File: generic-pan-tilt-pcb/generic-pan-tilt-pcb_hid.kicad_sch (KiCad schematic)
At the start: 10 parts, among them SW3 SW_DIP_x12, U5 MCP23017_SO

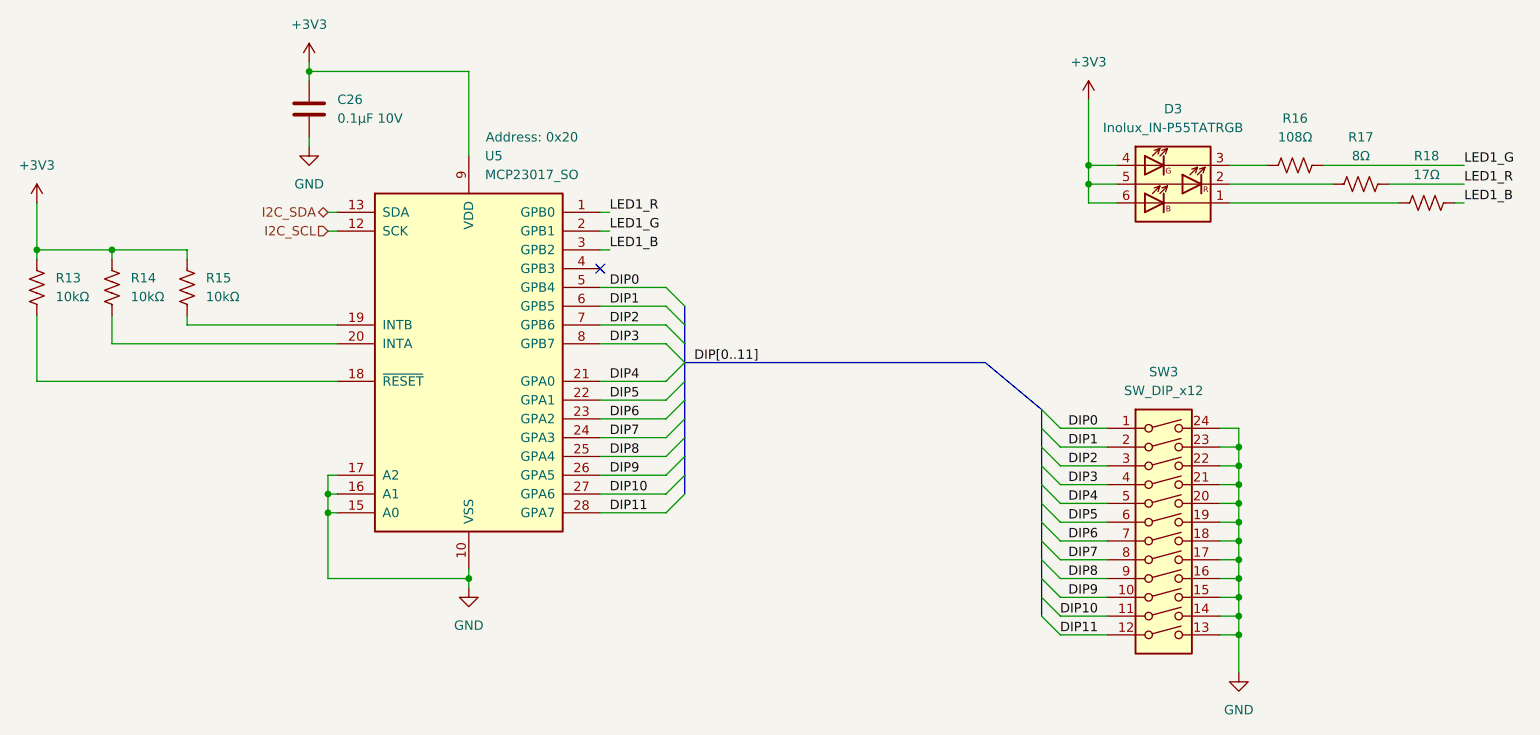
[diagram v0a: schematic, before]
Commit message: pick all footprints, begin layout
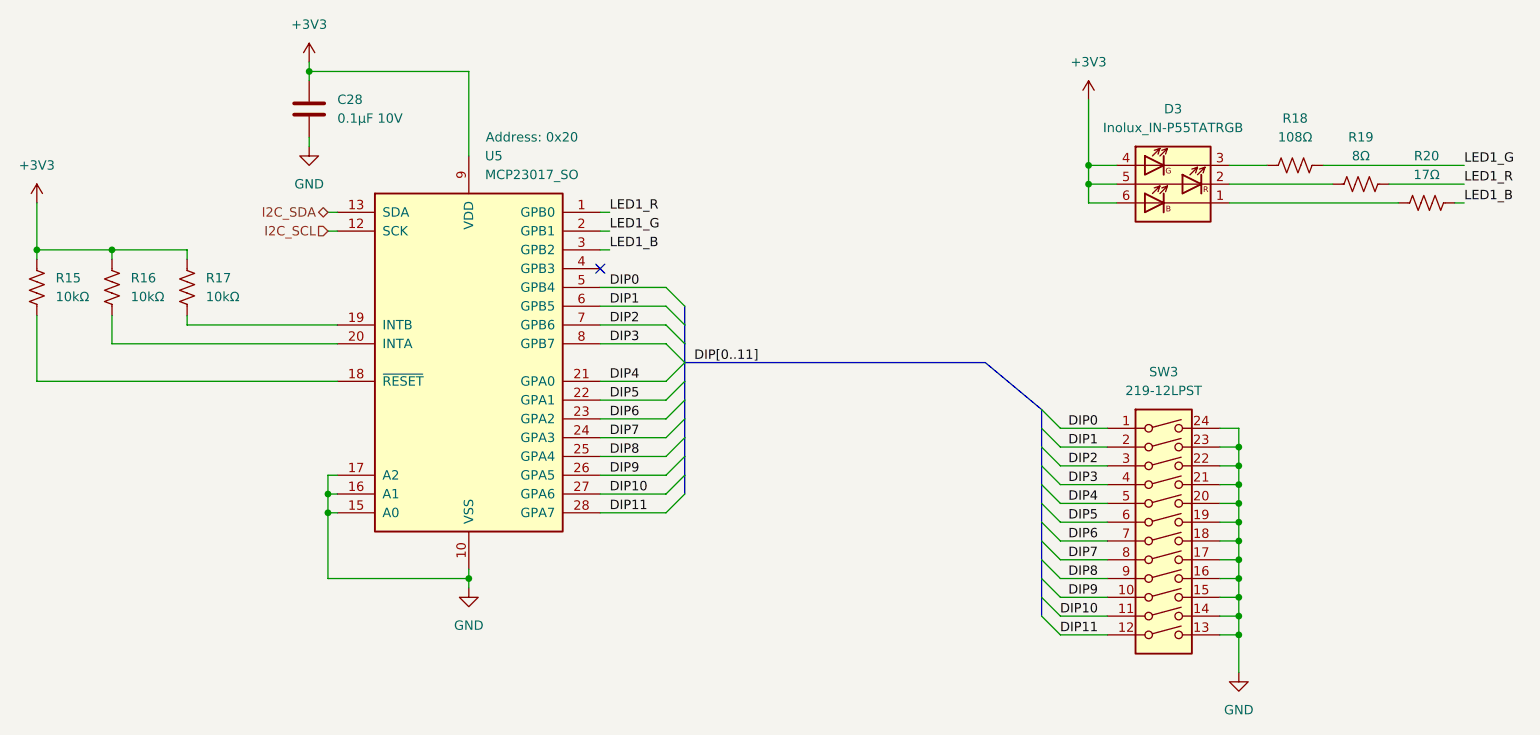
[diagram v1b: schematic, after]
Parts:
- C28: renamed from C26; footprint (none) -> Capacitor_SMD:C_0603_1608Metric
- R15: renamed from R13; footprint (none) -> Resistor_SMD:R_0603_1608Metric
- R16: renamed from R14; footprint (none) -> Resistor_SMD:R_0603_1608Metric
- R17: renamed from R15; footprint (none) -> Resistor_SMD:R_0603_1608Metric
- R18: renamed from R16; footprint (none) -> Resistor_SMD:R_0603_1608Metric
- R19: renamed from R17; footprint (none) -> Resistor_SMD:R_0603_1608Metric
- R20: renamed from R18; footprint (none) -> Resistor_SMD:R_0603_1608Metric
- SW3: value SW_DIP_x12 -> 219-12LPST; footprint (none) -> Button_Switch_SMD:SW_DIP_SPSTx12_Slide_6.7x32.04mm_W8.61mm_P2.54mm_LowProfile
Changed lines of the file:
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@@
 		(dnp no)
 		(fields_autoplaced yes)
-		(property "Reference" "R17"
+		(property "Reference" "R19"
 			(at 231.14 50.8 90)
 			(effects
@@
 			)
 		)
-		(property "Footprint" ""
+		(property "Footprint" "Resistor_SMD:R_0603_1608Metric"
 			(at 231.394 56.134 90)
 			(effects
@@
 			(project "generic-pan-tilt-pcb"
 				(path "/e3bbbe58-bf8f-42a8-8505-028de8235dc1/58e8aa21-838b-4e25-b5a5-dc2029ad2cce"
-					(reference "R17")
+					(reference "R19")
 					(unit 1)
 				)
@@
 		(dnp no)
 		(fields_autoplaced yes)
-		(property "Reference" "R15"
+		(property "Reference" "R17"
 			(at 74.93 69.8499 0)
 			(effects
@@
 			)
 		)
-		(property "Footprint" ""
+		(property "Footprint" "Resistor_SMD:R_0603_1608Metric"
 			(at 73.406 71.374 90)
 			(effects
@@
 			(project "generic-pan-tilt-pcb"
 				(path "/e3bbbe58-bf8f-42a8-8505-028de8235dc1/58e8aa21-838b-4e25-b5a5-dc2029ad2cce"
-					(reference "R15")
+					(reference "R17")
 					(unit 1)
 				)
@@
 		(dnp no)
 		(fields_autoplaced yes)
-		(property "Reference" "#PWR069"
+		(property "Reference" "#PWR068"
 			(at 214.63 129.54 0)
 			(effects
@@
 			(project "generic-pan-tilt-pcb"
 				(path "/e3bbbe58-bf8f-42a8-8505-028de8235dc1/58e8aa21-838b-4e25-b5a5-dc2029ad2cce"
-					(reference "#PWR069")
+					(reference "#PWR068")
 					(unit 1)
 				)
@@
 		(dnp no)
 		(fields_autoplaced yes)
-		(property "Reference" "#PWR067"
+		(property "Reference" "#PWR066"
 			(at 110.49 118.11 0)
 			(effects
@@
 			(project "generic-pan-tilt-pcb"
 				(path "/e3bbbe58-bf8f-42a8-8505-028de8235dc1/58e8aa21-838b-4e25-b5a5-dc2029ad2cce"
-					(reference "#PWR067")
+					(reference "#PWR066")
 					(unit 1)
 				)
@@
 			)
 		)
-		(property "Value" "SW_DIP_x12"
+		(property "Value" "219-12LPST"
 			(at 204.47 85.09 0)
 			(effects
@@
 			)
 		)
-		(property "Footprint" ""
+		(property "Footprint" "Button_Switch_SMD:SW_DIP_SPSTx12_Slide_6.7x32.04mm_W8.61mm_P2.54mm_LowProfile"
 			(at 204.47 105.41 0)
 			(effects
@@
 		(dnp no)
 		(fields_autoplaced yes)
-		(property "Reference" "#PWR065"
+		(property "Reference" "#PWR064"
 			(at 88.9 44.45 0)
 			(effects
@@
 			(project "generic-pan-tilt-pcb"
 				(path "/e3bbbe58-bf8f-42a8-8505-028de8235dc1/58e8aa21-838b-4e25-b5a5-dc2029ad2cce"
-					(reference "#PWR065")
+					(reference "#PWR064")
 					(unit 1)
 				)
@@
 		(dnp no)
 		(fields_autoplaced yes)
-		(property "Reference" "R13"
+		(property "Reference" "R15"
 			(at 54.61 69.8499 0)
 			(effects
@@
 			)
 		)
-		(property "Footprint" ""
+		(property "Footprint" "Resistor_SMD:R_0603_1608Metric"
 			(at 53.086 71.374 90)
 			(effects
@@
 			(project "generic-pan-tilt-pcb"
 				(path "/e3bbbe58-bf8f-42a8-8505-028de8235dc1/58e8aa21-838b-4e25-b5a5-dc2029ad2cce"
-					(reference "R13")
+					(reference "R15")
 					(unit 1)
 				)
@@
 		(dnp no)
 		(fields_autoplaced yes)
-		(property "Reference" "R16"
+		(property "Reference" "R18"
 			(at 222.25 48.26 90)
 			(effects
@@
 			)
 		)
-		(property "Footprint" ""
+		(property "Footprint" "Resistor_SMD:R_0603_1608Metric"
 			(at 221.996 55.626 90)
 			(effects
@@
 			(project "generic-pan-tilt-pcb"
 				(path "/e3bbbe58-bf8f-42a8-8505-028de8235dc1/58e8aa21-838b-4e25-b5a5-dc2029ad2cce"
-					(reference "R16")
+					(reference "R18")
 					(unit 1)
 				)
@@
 		(dnp no)
 		(fields_autoplaced yes)
-		(property "Reference" "#PWR068"
+		(property "Reference" "#PWR067"
 			(at 194.31 49.53 0)
 			(effects
@@
 			(project "generic-pan-tilt-pcb"
 				(path "/e3bbbe58-bf8f-42a8-8505-028de8235dc1/58e8aa21-838b-4e25-b5a5-dc2029ad2cce"
-					(reference "#PWR068")
+					(reference "#PWR067")
 					(unit 1)
 				)
@@
 		(dnp no)
 		(fields_autoplaced yes)
-		(property "Reference" "#PWR064"
+		(property "Reference" "#PWR063"
 			(at 52.07 63.5 0)
 			(effects
@@
 			(project "generic-pan-tilt-pcb"
 				(path "/e3bbbe58-bf8f-42a8-8505-028de8235dc1/58e8aa21-838b-4e25-b5a5-dc2029ad2cce"
-					(reference "#PWR064")
+					(reference "#PWR063")
 					(unit 1)
 				)
@@
 		(dnp no)
 		(fields_autoplaced yes)
-		(property "Reference" "C26"
+		(property "Reference" "C28"
 			(at 92.71 45.7199 0)
 			(effects
@@
 			)
 		)
-		(property "Footprint" ""
+		(property "Footprint" "Capacitor_SMD:C_0603_1608Metric"
 			(at 89.8652 50.8 0)
 			(effects
@@
 			(project "generic-pan-tilt-pcb"
 				(path "/e3bbbe58-bf8f-42a8-8505-028de8235dc1/58e8aa21-838b-4e25-b5a5-dc2029ad2cce"
-					(reference "C26")
+					(reference "C28")
 					(unit 1)
 				)
@@
 		(dnp no)
 		(fields_autoplaced yes)
-		(property "Reference" "R14"
+		(property "Reference" "R16"
 			(at 64.77 69.8499 0)
 			(effects
@@
 			)
 		)
-		(property "Footprint" ""
+		(property "Footprint" "Resistor_SMD:R_0603_1608Metric"
 			(at 63.246 71.374 90)
 			(effects
@@
 			(project "generic-pan-tilt-pcb"
 				(path "/e3bbbe58-bf8f-42a8-8505-028de8235dc1/58e8aa21-838b-4e25-b5a5-dc2029ad2cce"
-					(reference "R14")
+					(reference "R16")
 					(unit 1)
 				)
@@
 		(dnp no)
 		(fields_autoplaced yes)
-		(property "Reference" "#PWR066"
+		(property "Reference" "#PWR065"
 			(at 88.9 58.42 0)
 			(effects
@@
 			(project "generic-pan-tilt-pcb"
 				(path "/e3bbbe58-bf8f-42a8-8505-028de8235dc1/58e8aa21-838b-4e25-b5a5-dc2029ad2cce"
-					(reference "#PWR066")
+					(reference "#PWR065")
 					(unit 1)
 				)
@@
 		(dnp no)
 		(fields_autoplaced yes)
-		(property "Reference" "R18"
+		(property "Reference" "R20"
 			(at 240.03 53.34 90)
 			(effects
@@
 			)
 		)
-		(property "Footprint" ""
+		(property "Footprint" "Resistor_SMD:R_0603_1608Metric"
 			(at 240.284 58.674 90)
 			(effects
@@
 			(project "generic-pan-tilt-pcb"
 				(path "/e3bbbe58-bf8f-42a8-8505-028de8235dc1/58e8aa21-838b-4e25-b5a5-dc2029ad2cce"
-					(reference "R18")
-					(unit 1)
-				)
+					(reference "R20")
+					(unit 1)
+				)

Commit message: more progress
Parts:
- removed D3: Inolux_IN-P55TATRGB, LED_SMD:LED_Inolux_IN-P55TATRGB_PLCC6_5.0x5.5mm_P1.8mm, symbol LED:Inolux_IN-P55TATRGB
- removed R19: 8Ω, Resistor_SMD:R_0603_1608Metric, symbol Device:R_US
- added D3: LTST-C235KGKRKT, LED_SMD:LED_LiteOn_LTST-C235KGKRKT, symbol LED:LTST-C235KGKRKT
- renumbered R20 to R19
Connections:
- net +3V3: now also D3.2 (A2), D3.3 (A1)
- net LED1_G: now also R19.2; no longer R18.1
- net LED1_R: now also R18.1
- net at R18.2: now also D3.4 (K1)
- net at R19.1: now also D3.1 (K2)
- net LED1_B: no longer names the net of U5.3 (GPB2)
- net LED1_B: no longer R19.2
- no-connect marks 1 -> 2
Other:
- moved on the sheet: R19
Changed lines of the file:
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@@
-	)
-	(junction
-		(at 194.31 57.15)
-		(diameter 0)
-		(color 0 0 0 0)
 	)
 	(junction
@@
 		(at 128.27 68.58)
 	)
+	(no_connect
+		(at 128.27 66.04)
+	)
 	(bus_entry
 		(at 187.96 97.79)
@@
 	(wire
 		(pts
-			(xy 213.36 57.15) (xy 227.33 57.15)
-		)
-		(stroke
-			(width 0)
-			(type default)
-		)
-	)
-	(wire
-		(pts
 			(xy 88.9 40.64) (xy 88.9 41.91)
 		)
@@
 	(wire
 		(pts
-			(xy 226.06 54.61) (xy 245.11 54.61)
-		)
-		(stroke
-			(width 0)
-			(type default)
-		)
-	)
-	(wire
-		(pts
 			(xy 214.63 107.95) (xy 214.63 110.49)
 		)
@@
 	(wire
 		(pts
-			(xy 243.84 59.69) (xy 245.11 59.69)
+			(xy 232.41 59.69) (xy 233.68 59.69)
 		)
 		(stroke
@@
 	(wire
 		(pts
-			(xy 213.36 59.69) (xy 236.22 59.69)
+			(xy 213.36 59.69) (xy 224.79 59.69)
 		)
 		(stroke
@@
 	(wire
 		(pts
+			(xy 226.06 54.61) (xy 233.68 54.61)
+		)
+		(stroke
+			(width 0)
+			(type default)
+		)
+	)
+	(wire
+		(pts
 			(xy 128.27 91.44) (xy 137.16 91.44)
 		)
@@
 	(wire
 		(pts
-			(xy 234.95 57.15) (xy 245.11 57.15)
-		)
-		(stroke
-			(width 0)
-			(type default)
-		)
-	)
-	(wire
-		(pts
 			(xy 212.09 107.95) (xy 214.63 107.95)
 		)
@@
 	(wire
 		(pts
-			(xy 194.31 57.15) (xy 194.31 59.69)
+			(xy 194.31 54.61) (xy 194.31 59.69)
 		)
 		(stroke
@@
 		)
 	)
-	(wire
-		(pts
-			(xy 194.31 57.15) (xy 198.12 57.15)
-		)
-		(stroke
-			(width 0)
-			(type default)
-		)
-	)
 	(bus
 		(pts
@@
 	(wire
 		(pts
-			(xy 128.27 66.04) (xy 129.54 66.04)
-		)
-		(stroke
-			(width 0)
-			(type default)
-		)
-	)
-	(wire
-		(pts
 			(xy 128.27 83.82) (xy 137.16 83.82)
 		)
@@
 		(pts
 			(xy 212.09 92.71) (xy 214.63 92.71)
-		)
-		(stroke
-			(width 0)
-			(type default)
-		)
-	)
-	(wire
-		(pts
-			(xy 194.31 54.61) (xy 194.31 57.15)
 		)
 		(stroke
@@
 		)
 	)
-	(label "LED1_B"
-		(at 245.11 59.69 0)
-		(fields_autoplaced yes)
-		(effects
-			(font
-				(size 1.27 1.27)
-			)
-			(justify left bottom)
-		)
-	)
 	(label "DIP9"
 		(at 129.54 96.52 0)
@@
 		)
 	)
-	(label "LED1_B"
-		(at 129.54 66.04 0)
-		(fields_autoplaced yes)
-		(effects
-			(font
-				(size 1.27 1.27)
-			)
-			(justify left bottom)
-		)
-	)
 	(label "DIP8"
 		(at 129.54 93.98 0)
@@
 	)
 	(label "LED1_G"
-		(at 245.11 54.61 0)
+		(at 233.68 59.69 0)
 		(fields_autoplaced yes)
 		(effects
@@
 	)
 	(label "LED1_R"
-		(at 245.11 57.15 0)
+		(at 233.68 54.61 0)
 		(fields_autoplaced yes)
 		(effects
@@
 			)
 			(justify right)
-		)
-	)
-	(symbol
-		(lib_id "Device:R_US")
-		(at 231.14 57.15 90)
-		(unit 1)
-		(exclude_from_sim no)
-		(in_bom yes)
-		(on_board yes)
-		(dnp no)
-		(fields_autoplaced yes)
-		(property "Reference" "R19"
-			(at 231.14 50.8 90)
-			(effects
-				(font
-					(size 1.27 1.27)
-				)
-			)
-		)
-		(property "Value" "8Ω"
-			(at 231.14 53.34 90)
-			(effects
-				(font
-					(size 1.27 1.27)
-				)
-			)
-		)
-		(property "Footprint" "Resistor_SMD:R_0603_1608Metric"
-			(at 231.394 56.134 90)
-			(effects
-				(font
-					(size 1.27 1.27)
-				)
-				(hide yes)
-			)
-		)
-		(property "Datasheet" "~"
-			(at 231.14 57.15 0)
-			(effects
-				(font
-					(size 1.27 1.27)
-				)
-				(hide yes)
-			)
-		)
-		(property "Description" "Resistor, US symbol"
-			(at 231.14 57.15 0)
-			(effects
-				(font
-					(size 1.27 1.27)
-				)
-				(hide yes)
-			)
-		)
-		(pin "1"
-		)
-		(pin "2"
-		)
-		(instances
-			(project "generic-pan-tilt-pcb"
-				(path "/e3bbbe58-bf8f-42a8-8505-028de8235dc1/58e8aa21-838b-4e25-b5a5-dc2029ad2cce"
-					(reference "R19")
-					(unit 1)
-				)
-			)
 		)
 	)
@@
 				(path "/e3bbbe58-bf8f-42a8-8505-028de8235dc1/58e8aa21-838b-4e25-b5a5-dc2029ad2cce"
 					(reference "R17")
+					(unit 1)
+				)
+			)
+		)
+	)
+	(symbol
+		(lib_id "LED:LTST-C235KGKRKT")
+		(at 205.74 57.15 0)
+		(unit 1)
+		(exclude_from_sim no)
+		(in_bom yes)
+		(on_board yes)
+		(dnp no)
+		(fields_autoplaced yes)
+		(property "Reference" "D3"
+			(at 205.74 45.72 0)
+			(effects
+				(font
+					(size 1.27 1.27)
+				)
+			)
+		)
+		(property "Value" "LTST-C235KGKRKT"
+			(at 205.74 48.26 0)
+			(effects
+				(font
+					(size 1.27 1.27)
+				)
+			)
+		)
+		(property "Footprint" "LED_SMD:LED_LiteOn_LTST-C235KGKRKT"
+			(at 206.502 57.15 0)
+			(effects
+				(font
+					(size 1.27 1.27)
+				)
+				(hide yes)
+			)
+		)
+		(property "Datasheet" "https://optoelectronics.liteon.com/upload/download/DS22-2009-0219/LTST-C235KGKRKT.pdf"
+			(at 206.502 57.15 0)
+			(effects
+				(font
+					(size 1.27 1.27)
+				)
+				(hide yes)
+			)
+		)
+		(property "Description" "LED dual red/green, 4-pin, down-facing"
+			(at 205.74 57.15 0)
+			(effects
+				(font
+					(size 1.27 1.27)
+				)
+				(hide yes)
+			)
+		)
+		(pin "2"
+		)
+		(pin "1"
+		)
+		(pin "4"
+		)
+		(pin "3"
+		)
+		(instances
+			(project ""
+				(path "/e3bbbe58-bf8f-42a8-8505-028de8235dc1/58e8aa21-838b-4e25-b5a5-dc2029ad2cce"
+					(reference "D3")
 					(unit 1)
 				)
@@
 	)
 	(symbol
-		(lib_id "LED:Inolux_IN-P55TATRGB")
-		(at 205.74 57.15 0)
-		(unit 1)
-		(exclude_from_sim no)
-		(in_bom yes)
-		(on_board yes)
-		(dnp no)
-		(fields_autoplaced yes)
-		(property "Reference" "D3"
-			(at 205.74 46.99 0)
-			(effects
-				(font
-					(size 1.27 1.27)
-				)
-			)
-		)
-		(property "Value" "Inolux_IN-P55TATRGB"
-			(at 205.74 49.53 0)
-			(effects
-				(font
-					(size 1.27 1.27)
-				)
-			)
-		)
-		(property "Footprint" "LED_SMD:LED_Inolux_IN-P55TATRGB_PLCC6_5.0x5.5mm_P1.8mm"
-			(at 200.66 65.278 0)
-			(effects
-				(font
-					(size 1.27 1.27)
-				)
-				(justify left)
-				(hide yes)
-			)
-		)
-		(property "Datasheet" "https://www.inolux-corp.com/datasheet/SMDLED/RGB%20Top%20View/IN-P55TATRGB.pdf"
-			(at 200.66 67.31 0)
-			(effects
-				(font
-					(size 1.27 1.27)
-				)
-				(justify left)
-				(hide yes)
-			)
-		)
-		(property "Description" "Inolux RGB LED, PLCC-6"
-			(at 205.74 57.15 0)
-			(effects
-				(font
-					(size 1.27 1.27)
-				)
-				(hide yes)
-			)
-		)
-		(pin "1"
-		)
-		(pin "4"
-		)
-		(pin "5"
-		)
-		(pin "3"
-		)
-		(pin "2"
-		)
-		(pin "6"
-		)
-		(instances
-			(project "generic-pan-tilt-pcb"
-				(path "/e3bbbe58-bf8f-42a8-8505-028de8235dc1/58e8aa21-838b-4e25-b5a5-dc2029ad2cce"
-					(reference "D3")
-					(unit 1)
-				)
-			)
-		)
-	)
-	(symbol
 		(lib_id "Device:C")
 		(at 88.9 46.99 0)
@@
 	(symbol
 		(lib_id "Device:R_US")
-		(at 240.03 59.69 90)
+		(at 228.6 59.69 90)
 		(unit 1)
 		(exclude_from_sim no)
@@
 		(dnp no)
 		(fields_autoplaced yes)
-		(property "Reference" "R20"
-			(at 240.03 53.34 90)
+		(property "Reference" "R19"
+			(at 228.6 53.34 90)
 			(effects
 				(font
@@
 		)
 		(property "Value" "17Ω"
-			(at 240.03 55.88 90)
+			(at 228.6 55.88 90)
 			(effects
 				(font
@@
 		)
 		(property "Footprint" "Resistor_SMD:R_0603_1608Metric"
-			(at 240.284 58.674 90)
+			(at 228.854 58.674 90)
 			(effects
 				(font
@@
 		)
 		(property "Datasheet" "~"
-			(at 240.03 59.69 0)
+			(at 228.6 59.69 0)
 			(effects
 				(font
@@
 		)
 		(property "Description" "Resistor, US symbol"
-			(at 240.03 59.69 0)
+			(at 228.6 59.69 0)
 			(effects
 				(font
@@
 			(project "generic-pan-tilt-pcb"
 				(path "/e3bbbe58-bf8f-42a8-8505-028de8235dc1/58e8aa21-838b-4e25-b5a5-dc2029ad2cce"
-					(reference "R20")
+					(reference "R19")
 					(unit 1)
 				)

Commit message: begin new routing
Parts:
- C28: footprint Capacitor_SMD:C_0603_1608Metric -> Capacitor_SMD:C_0402_1005Metric
- R15, R16, R17, R18, R19: footprint Resistor_SMD:R_0603_1608Metric -> Capacitor_SMD:C_0402_1005Metric
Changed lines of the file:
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@@
 			)
 		)
-		(property "Footprint" "Resistor_SMD:R_0603_1608Metric"
+		(property "Footprint" "Capacitor_SMD:C_0402_1005Metric"
 			(at 73.406 71.374 90)
 			(effects
@@
 			)
 		)
-		(property "Footprint" "Resistor_SMD:R_0603_1608Metric"
+		(property "Footprint" "Capacitor_SMD:C_0402_1005Metric"
 			(at 53.086 71.374 90)
 			(effects
@@
 			)
 		)
-		(property "Footprint" "Resistor_SMD:R_0603_1608Metric"
+		(property "Footprint" "Capacitor_SMD:C_0402_1005Metric"
 			(at 221.996 55.626 90)
 			(effects
@@
 			)
 		)
-		(property "Footprint" "Capacitor_SMD:C_0603_1608Metric"
+		(property "Footprint" "Capacitor_SMD:C_0402_1005Metric"
 			(at 89.8652 50.8 0)
 			(effects
@@
 			)
 		)
-		(property "Footprint" "Resistor_SMD:R_0603_1608Metric"
+		(property "Footprint" "Capacitor_SMD:C_0402_1005Metric"
 			(at 63.246 71.374 90)
 			(effects
@@
 			)
 		)
-		(property "Footprint" "Resistor_SMD:R_0603_1608Metric"
+		(property "Footprint" "Capacitor_SMD:C_0402_1005Metric"
 			(at 228.854 58.674 90)
 			(effects

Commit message: more pcb, kicost maf digikey mouser
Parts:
- D3: digikey# (none) -> 160-2026-1-ND; manf# (none) -> LTST-C235KGKRKT; mouser# (none) -> 859-LTST-C235KGKRKT
- SW3: digikey# (none) -> CT21912LPST-ND; manf# (none) -> 219-12LPST; mouser# (none) -> 774-21912LPST
- U5: digikey# (none) -> MCP23017T-E/SOCT-ND; manf# (none) -> MCP23017T-E/SO; mouser# (none) -> 579-MCP23017T-E/SO
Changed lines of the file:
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@@
+			)
+		)
+		(property "digikey#" "160-2026-1-ND"
+			(at 205.74 57.15 0)
+			(effects
+				(font
+					(size 1.27 1.27)
+				)
+				(hide yes)
+			)
+		)
+		(property "manf#" "LTST-C235KGKRKT"
+			(at 205.74 57.15 0)
+			(effects
+				(font
+					(size 1.27 1.27)
+				)
+				(hide yes)
+			)
+		)
+		(property "mouser#" "859-LTST-C235KGKRKT"
+			(at 205.74 57.15 0)
+			(effects
+				(font
+					(size 1.27 1.27)
+				)
+				(hide yes)
 			)
 		)
@@
 			)
 		)
+		(property "digikey#" "CT21912LPST-ND"
+			(at 204.47 105.41 0)
+			(effects
+				(font
+					(size 1.27 1.27)
+				)
+				(hide yes)
+			)
+		)
+		(property "manf#" "219-12LPST"
+			(at 204.47 105.41 0)
+			(effects
+				(font
+					(size 1.27 1.27)
+				)
+				(hide yes)
+			)
+		)
+		(property "mouser#" "774-21912LPST"
+			(at 204.47 105.41 0)
+			(effects
+				(font
+					(size 1.27 1.27)
+				)
+				(hide yes)
+			)
+		)
 		(pin "6"
 		)
@@
 			)
 		)
+		(property "digikey#" "MCP23017T-E/SOCT-ND"
+			(at 110.49 81.28 0)
+			(effects
+				(font
+					(size 1.27 1.27)
+				)
+				(hide yes)
+			)
+		)
+		(property "manf#" "MCP23017T-E/SO"
+			(at 110.49 81.28 0)
+			(effects
+				(font
+					(size 1.27 1.27)
+				)
+				(hide yes)
+			)
+		)
+		(property "mouser#" "579-MCP23017T-E/SO"
+			(at 110.49 81.28 0)
+			(effects
+				(font
+					(size 1.27 1.27)
+				)
+				(hide yes)
+			)
+		)

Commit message: dippity dip dip dip chip
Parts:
- SW3: footprint Button_Switch_SMD:SW_DIP_SPSTx12_Slide_6.7x32.04mm_W8.61mm_P2.54mm_LowProfile -> Button_Switch_THT:SW_DIP_SPSTx12_Slide_9.78x32.66mm_W7.62mm_P2.54mm
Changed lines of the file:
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@@
 			)
 		)
-		(property "Footprint" "Button_Switch_SMD:SW_DIP_SPSTx12_Slide_6.7x32.04mm_W8.61mm_P2.54mm_LowProfile"
+		(property "Footprint" "Button_Switch_THT:SW_DIP_SPSTx12_Slide_9.78x32.66mm_W7.62mm_P2.54mm"
 			(at 204.47 105.41 0)
 			(effects
